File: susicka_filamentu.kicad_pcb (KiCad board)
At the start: 4 copper layers, 55 parts, among them J2 Conn_01x03, J3 Conn_01x04, J4 PJ-102AH, J5 Screw_Terminal_01x02, J6 Conn_01x04, J7 Conn_01x04, Q1 Q_NMOS_GSD, U1 RP2350A-QFN60, U2 RM2, U3 W25Q128JVS, U4 AP63203WU, Y1 Crystal_GND24

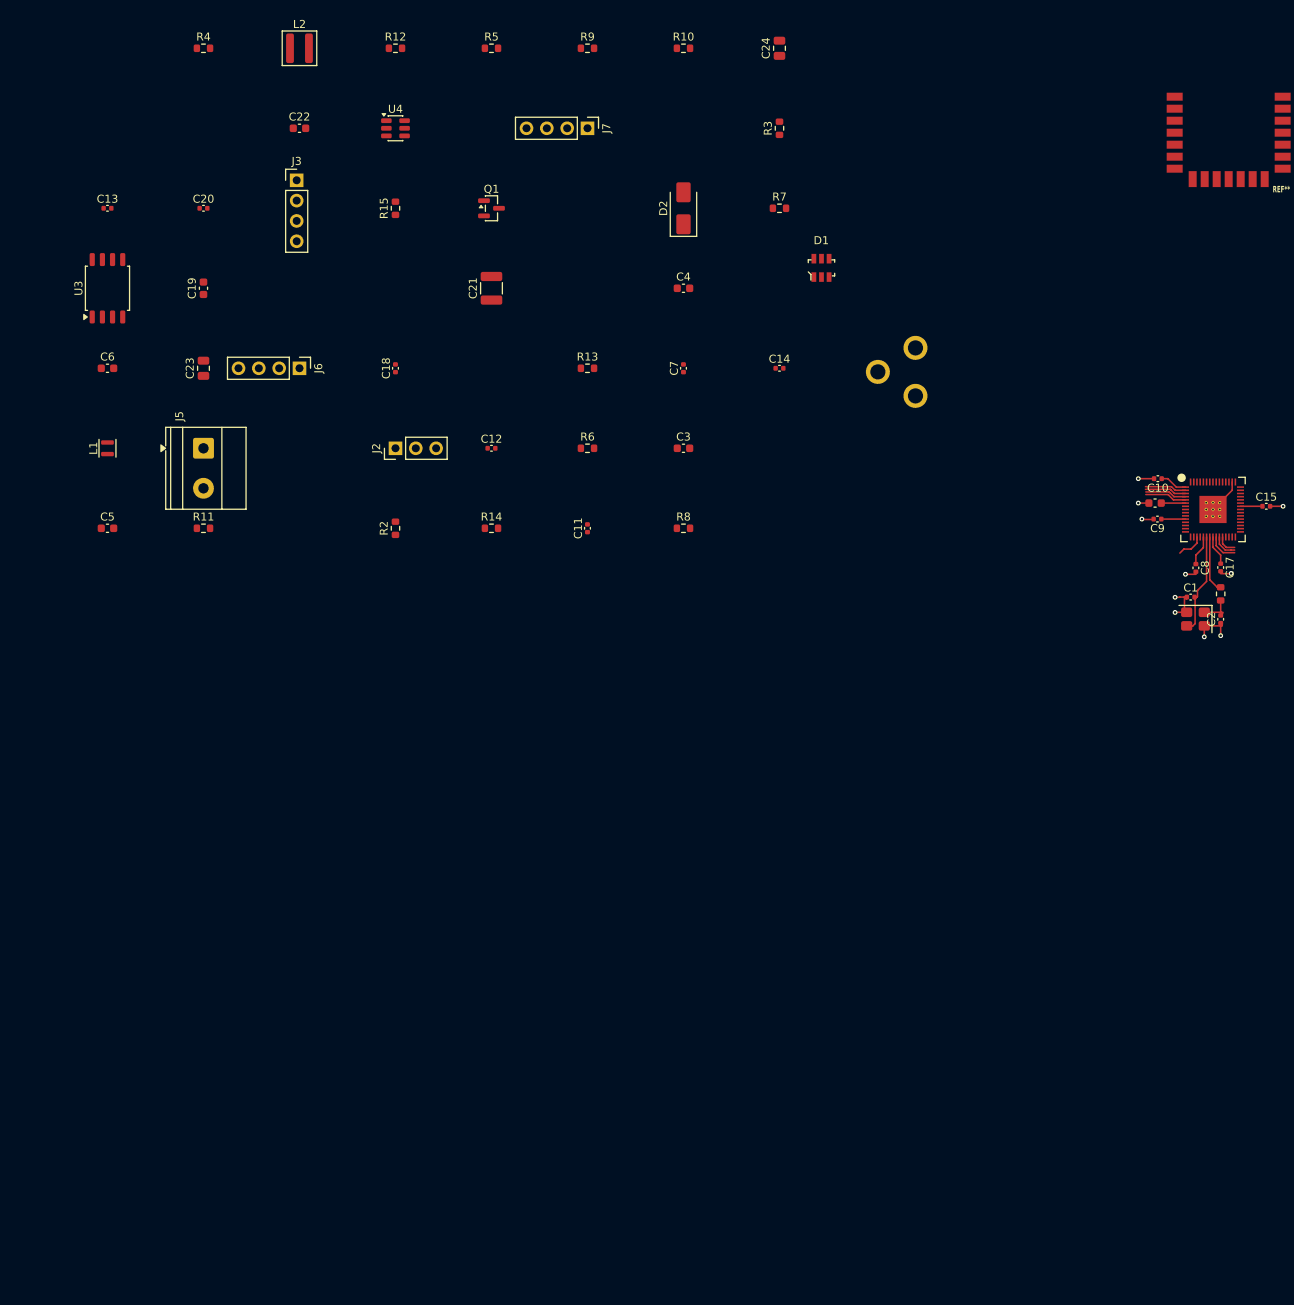
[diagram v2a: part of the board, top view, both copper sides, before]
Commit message: Add communication test points, tidy root sheet, board setup
- Test points TP6-TP19 (1 mm pads) on I2C1, I2C0, HX711, RM2 gSPI,
  heater/fan/exhaust PWM and NTC ADC, plus TP12 GND loop
- Root sheet: GPIO2-5 -> J6/J7 and GPIO24/25/29 -> RM2 now connected by
  global labels (HX711_DT/SCK, WL_DATA/CS/CLK), J6 moved
- Board updated from schematic (F8)
- Board setup: min through-hole 0.2 mm (0.25 mm vias under RP2350),
  new net class Power (1.5 mm track, 0.3 mm clearance, 0.8/0.4 via)
  for 24V_IN, 24V, fuse/heater nets

Co-Authored-By: Claude Opus 5.5 <noreply@anthropic.com>
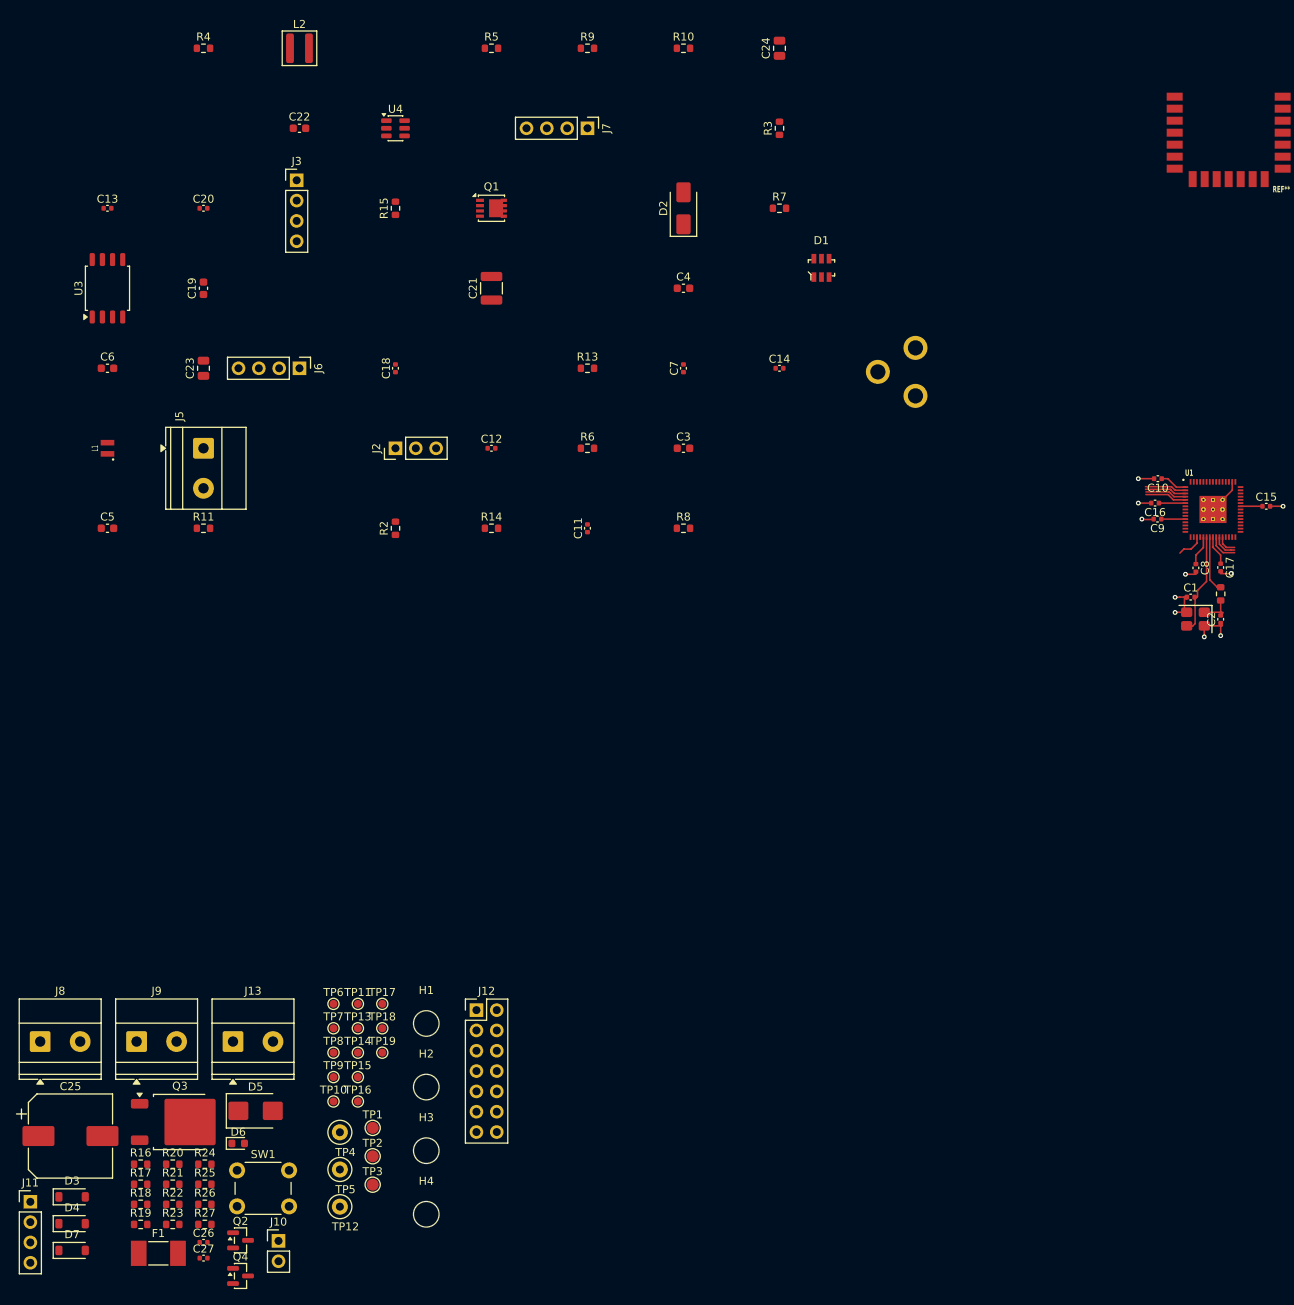
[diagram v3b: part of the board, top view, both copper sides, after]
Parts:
- removed R12: 10k, Resistor_SMD:R_0603_1608Metric
- added C25: 100uF 50V, Capacitor_SMD:CP_Elec_10x10, F.Cu at (25.0, 162.2)
- added C26: 100nF, Capacitor_SMD:C_0402_1005Metric, F.Cu at (41.7, 175.5)
- added C27: 100nF, Capacitor_SMD:C_0402_1005Metric, F.Cu at (41.7, 177.5)
- added D3: B5819W, Diode_SMD:D_SOD-123, F.Cu at (25.2, 169.8)
- added D4: BZT52C15, Diode_SMD:D_SOD-123, F.Cu at (25.2, 173.2)
- added D5: SMBJ24CA, Diode_SMD:D_SMB, F.Cu at (48.2, 159.1)
- added D6: LED zelená, LED_SMD:LED_0603_1608Metric, F.Cu at (46.0, 163.1)
- added D7: B5819W, Diode_SMD:D_SOD-123, F.Cu at (25.2, 176.5)
- added F1: 4A T, Fuse:Fuse_Littelfuse-NANO2-451_453, F.Cu at (36.0, 176.9)
- added H1: M3, MountingHole:MountingHole_3.2mm_M3, F.Cu at (69.5, 148.2)
- added H2: M3, MountingHole:MountingHole_3.2mm_M3, F.Cu at (69.5, 156.1)
- added H3: M3, MountingHole:MountingHole_3.2mm_M3, F.Cu at (69.5, 164.1)
- added H4: M3, MountingHole:MountingHole_3.2mm_M3, F.Cu at (69.5, 172.0)
- added J10: NTC 100k B3950, Connector_PinHeader_2.54mm:PinHeader_1x02_P2.54mm_Vertical, F.Cu at (51.0, 175.3)
- added J11: SHT40 #2, Connector_PinHeader_2.54mm:PinHeader_1x04_P2.54mm_Vertical, F.Cu at (20.0, 170.4)
- added J12: GPIO rezerva, Connector_PinHeader_2.54mm:PinHeader_2x07_P2.54mm_Vertical, F.Cu at (75.8, 146.5)
- added J13: Tepelna pojistka, TerminalBlock_Phoenix:TerminalBlock_Phoenix_MKDS-1,5-2_1x02_P5.00mm_Horizontal, F.Cu at (45.3, 150.4)
- added J8: Ventilator 24V, TerminalBlock_Phoenix:TerminalBlock_Phoenix_MKDS-1,5-2_1x02_P5.00mm_Horizontal, F.Cu at (21.2, 150.4)
- added J9: Odtah 24V, TerminalBlock_Phoenix:TerminalBlock_Phoenix_MKDS-1,5-2_1x02_P5.00mm_Horizontal, F.Cu at (33.3, 150.4)
- added Q2: AO3422, Package_TO_SOT_SMD:SOT-23, F.Cu at (46.3, 175.3)
- added Q3: AOD4185, Package_TO_SOT_SMD:TO-252-2, F.Cu at (38.7, 160.5)
- added Q4: AO3422, Package_TO_SOT_SMD:SOT-23, F.Cu at (46.3, 179.7)
- added R16: 100, Resistor_SMD:R_0603_1608Metric, F.Cu at (33.8, 165.7)
- added R17: 100, Resistor_SMD:R_0603_1608Metric, F.Cu at (33.8, 168.2)
- added R18: 100k, Resistor_SMD:R_0603_1608Metric, F.Cu at (33.8, 170.8)
- added R19: 10k, Resistor_SMD:R_0603_1608Metric, F.Cu at (33.8, 173.3)
- added R20: 1k, Resistor_SMD:R_0603_1608Metric, F.Cu at (37.8, 165.7)
- added R21: 4k7, Resistor_SMD:R_0603_1608Metric, F.Cu at (37.8, 168.2)
- added R22: 4k7, Resistor_SMD:R_0603_1608Metric, F.Cu at (37.8, 170.8)
- added R23: 100, Resistor_SMD:R_0603_1608Metric, F.Cu at (37.8, 173.3)
- added R24: 100k, Resistor_SMD:R_0603_1608Metric, F.Cu at (41.8, 165.7)
- added R25: 22k, Resistor_SMD:R_0603_1608Metric, F.Cu at (41.8, 168.2)
- added R26: 4k7, Resistor_SMD:R_0603_1608Metric, F.Cu at (41.8, 170.8)
- added R27: 4k7, Resistor_SMD:R_0603_1608Metric, F.Cu at (41.8, 173.3)
- added SW1: Tlacitko, Button_Switch_THT:SW_PUSH_6mm, F.Cu at (45.9, 166.5)
- added TP1: 24V, TestPoint:TestPoint_Pad_D1.5mm, F.Cu at (62.8, 161.2)
- added TP10: HX711_DT, TestPoint:TestPoint_Pad_D1.0mm, F.Cu at (57.9, 157.9)
- added TP11: HX711_SCK, TestPoint:TestPoint_Pad_D1.0mm, F.Cu at (61.0, 145.7)
- added TP12: GND, TestPoint:TestPoint_Loop_D2.50mm_Drill1.0mm, F.Cu at (58.7, 171.1)
- added TP13: WL_CLK, TestPoint:TestPoint_Pad_D1.0mm, F.Cu at (61.0, 148.8)
- added TP14: WL_CS, TestPoint:TestPoint_Pad_D1.0mm, F.Cu at (61.0, 151.8)
- added TP15: WL_DATA, TestPoint:TestPoint_Pad_D1.0mm, F.Cu at (61.0, 154.8)
- added TP16: HEAT_PWM, TestPoint:TestPoint_Pad_D1.0mm, F.Cu at (61.0, 157.9)
- added TP17: FAN_PWM, TestPoint:TestPoint_Pad_D1.0mm, F.Cu at (64.0, 145.7)
- added TP18: EXH_PWM, TestPoint:TestPoint_Pad_D1.0mm, F.Cu at (64.0, 148.8)
- added TP19: NTC_ADC, TestPoint:TestPoint_Pad_D1.0mm, F.Cu at (64.0, 151.8)
- added TP2: +3V3, TestPoint:TestPoint_Pad_D1.5mm, F.Cu at (62.8, 164.8)
- added TP3: +1V1, TestPoint:TestPoint_Pad_D1.5mm, F.Cu at (62.8, 168.3)
- added TP4: GND, TestPoint:TestPoint_Loop_D2.50mm_Drill1.0mm, F.Cu at (58.7, 161.8)
- added TP5: GND, TestPoint:TestPoint_Loop_D2.50mm_Drill1.0mm, F.Cu at (58.7, 166.4)
- added TP6: SDA, TestPoint:TestPoint_Pad_D1.0mm, F.Cu at (57.9, 145.7)
- added TP7: SCL, TestPoint:TestPoint_Pad_D1.0mm, F.Cu at (57.9, 148.8)
- added TP8: SDA0, TestPoint:TestPoint_Pad_D1.0mm, F.Cu at (57.9, 151.8)
- added TP9: SCL0, TestPoint:TestPoint_Pad_D1.0mm, F.Cu at (57.9, 154.8)
- C16: value 4,7 uF -> 100 nF; footprint Capacitor_SMD:C_0603_1608Metric -> Capacitor_SMD:C_0402_1005Metric
- J5: value Screw_Terminal_01x02 -> Topeni 24V
- J6: value Conn_01x04 -> SHT4x
- J7: value Conn_01x04 -> HX711
- L1: footprint Inductor_SMD:L_Murata_DFE201610P -> rp2350A_QFN60:L_Abracon_AOTA-B201610
- L2: value 3,9 uH -> 4,7uH
- Q1: value Q_NMOS_GSD -> SiS434DN; footprint Package_TO_SOT_SMD:SOT-23 -> susicka:Vishay_PowerPAK_1212-8_Single_GSD
- R15: value R -> 100k
- U1: footprint rp2350A_QFN60:RP2350A_QFN-60_EP_7.75x7.75_Pitch0.4mm -> rp2350A_QFN60:RP2350A_QFN-60_RPi_Minimal
- Y1: value Crystal_GND24 -> ABM8-272-T3 12MHz
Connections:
- net /RM2/RM2_CS renamed WL_CS
- net /RM2/RM2_DI renamed WL_DATA
- net /RM2/RM2_SCLK renamed WL_CLK
- net Net-(J6-Pin_3) renamed SDA
- net Net-(J6-Pin_4) renamed SCL
- net Net-(J7-Pin_3) renamed HX711_DT
- net Net-(J7-Pin_4) renamed HX711_SCK
- D2 pad 1: (no net) -> /vystupy/HEAT_V
- D2 pad 2: (no net) -> Net-(D2-A)
- J4 pad 1: 24V -> 24V_IN
- J5 pad 1: 24V -> Net-(D2-A)
- J5 pad 2: Net-(J5-Pin_2) -> /vystupy/HEAT_V
- Q1 pad 1: /GPIO14 -> Net-(Q1-G)
- Q1 pad 3: Net-(J5-Pin_2) -> Net-(D2-A)
- R15 pad 1: /GPIO14 -> Net-(Q1-G)
- U1 pad 12: unconnected-(U1-GPIO8-Pad12) -> SDA0
- U1 pad 13: unconnected-(U1-GPIO9-Pad13) -> SCL0
- U1 pad 14: unconnected-(U1-GPIO10-Pad14) -> GP10
- U1 pad 15: unconnected-(U1-GPIO11-Pad15) -> GP11
- U1 pad 16: unconnected-(U1-GPIO12-Pad16) -> EXH_PWM
- U1 pad 17: unconnected-(U1-GPIO13-Pad17) -> FAN_PWM
- U1 pad 18: /GPIO14 -> HEAT_PWM
- U1 pad 19: unconnected-(U1-GPIO15-Pad19) -> BTN
- U1 pad 27: unconnected-(U1-GPIO16-Pad27) -> GP16
- U1 pad 28: unconnected-(U1-GPIO17-Pad28) -> GP17
- U1 pad 29: unconnected-(U1-GPIO18-Pad29) -> GP18
- U1 pad 31: unconnected-(U1-GPIO19-Pad31) -> GP19
- U1 pad 32: unconnected-(U1-GPIO20-Pad32) -> GP20
- U1 pad 33: unconnected-(U1-GPIO21-Pad33) -> GP21
- U1 pad 34: unconnected-(U1-GPIO22-Pad34) -> GP22
- U1 pad 40: unconnected-(U1-GPIO26_ADC0-Pad40) -> NTC_ADC
- U1 pad 41: unconnected-(U1-GPIO27_ADC1-Pad41) -> GP27
- U1 pad 42: unconnected-(U1-GPIO28_ADC2-Pad42) -> GP28
- U2 pad 8: unconnected-(U2-GPIO0-Pad8) -> WL_GPIO0
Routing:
- net HEAT_PWM: track 0.00 -> 3.43 mm
- net /GPIO14: track 3.43 -> 0.00 mm

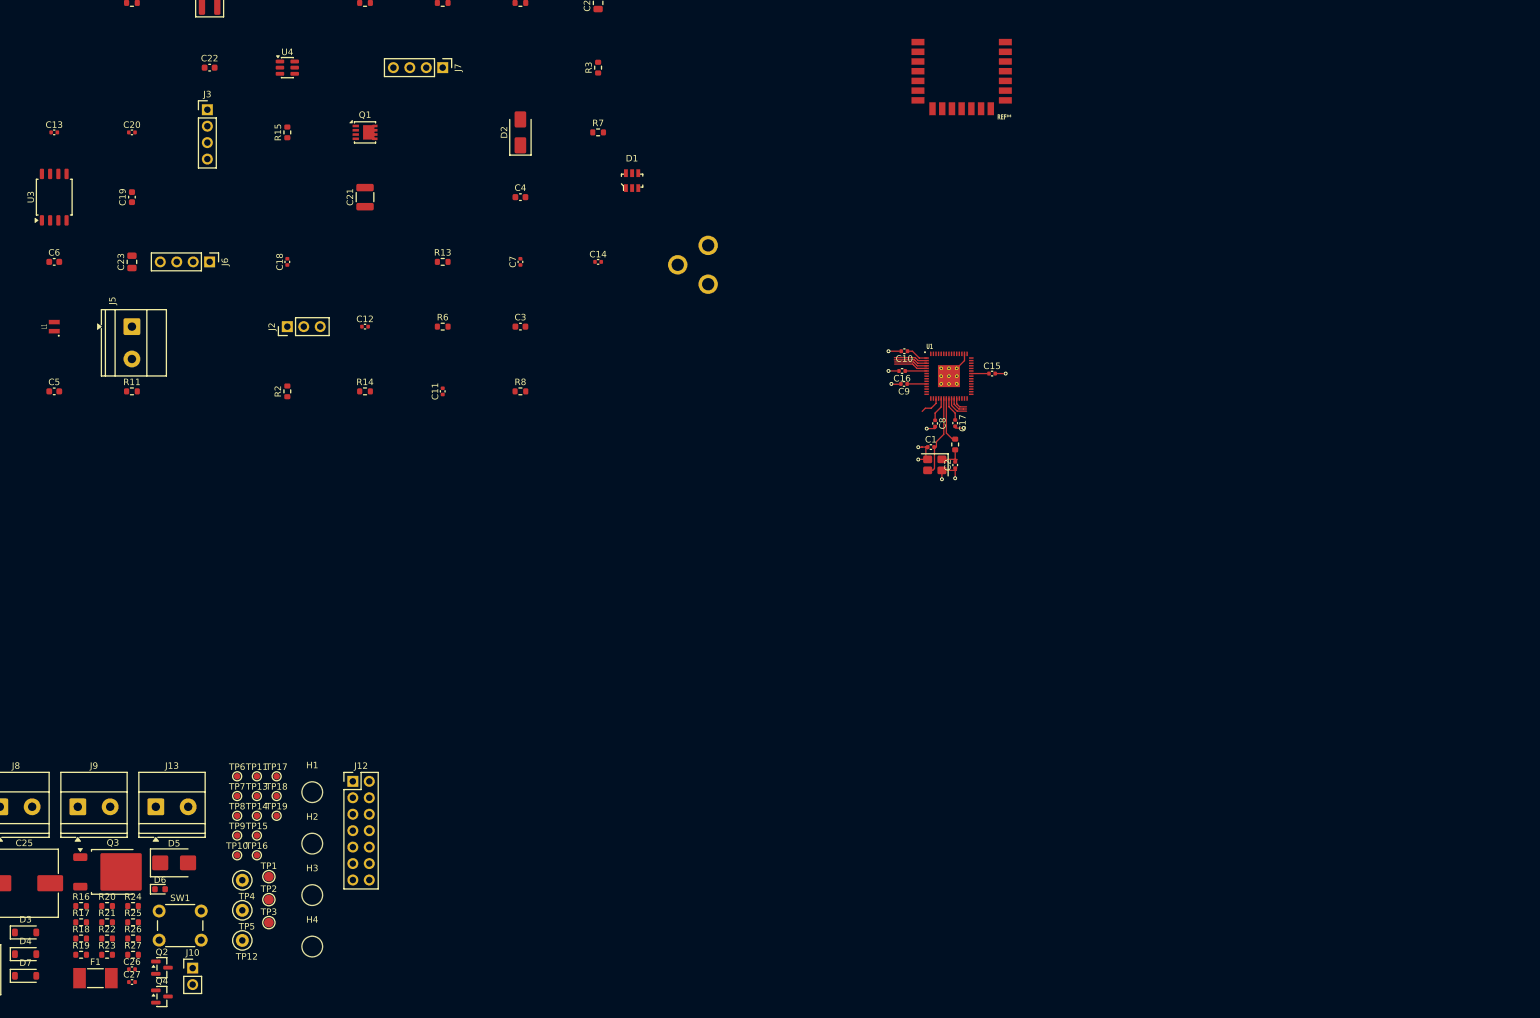
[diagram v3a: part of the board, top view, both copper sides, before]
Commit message: Layout progress, VREG per reference, SI simulation, project notes
- Board: 70x100 mm outline, mounting holes, crystal, RP2350 decoupling,
  VREG copied from RP2350A Minimal R4 (zones, priorities, PGND track),
  RM2 placement and gSPI routing (CLK 16.5 mm, DATA 14.4 mm),
  RF keep-out rule area on all copper layers, test points TP12-TP15
- C4/C5/C6/R7 in 0402; C5/C6 use susicka:C_0402_1005Metric_RPi
  (0.56 mm pad gap so VREG_LX passes under the caps)
- simulace/wl_clk: KiCad ngspice model of WL_CLK (TLINE Z0 ~94 ohm,
  td ~96 ps) for transient and AC (Bode) analysis
- CLAUDE.md and Claude subagents (.claude/agents) moved into the PCB
  branch so the project context is available on other machines
- Ignore KiCad #auto_saved_files#

Co-Authored-By: Claude Opus 5.5 <noreply@anthropic.com>
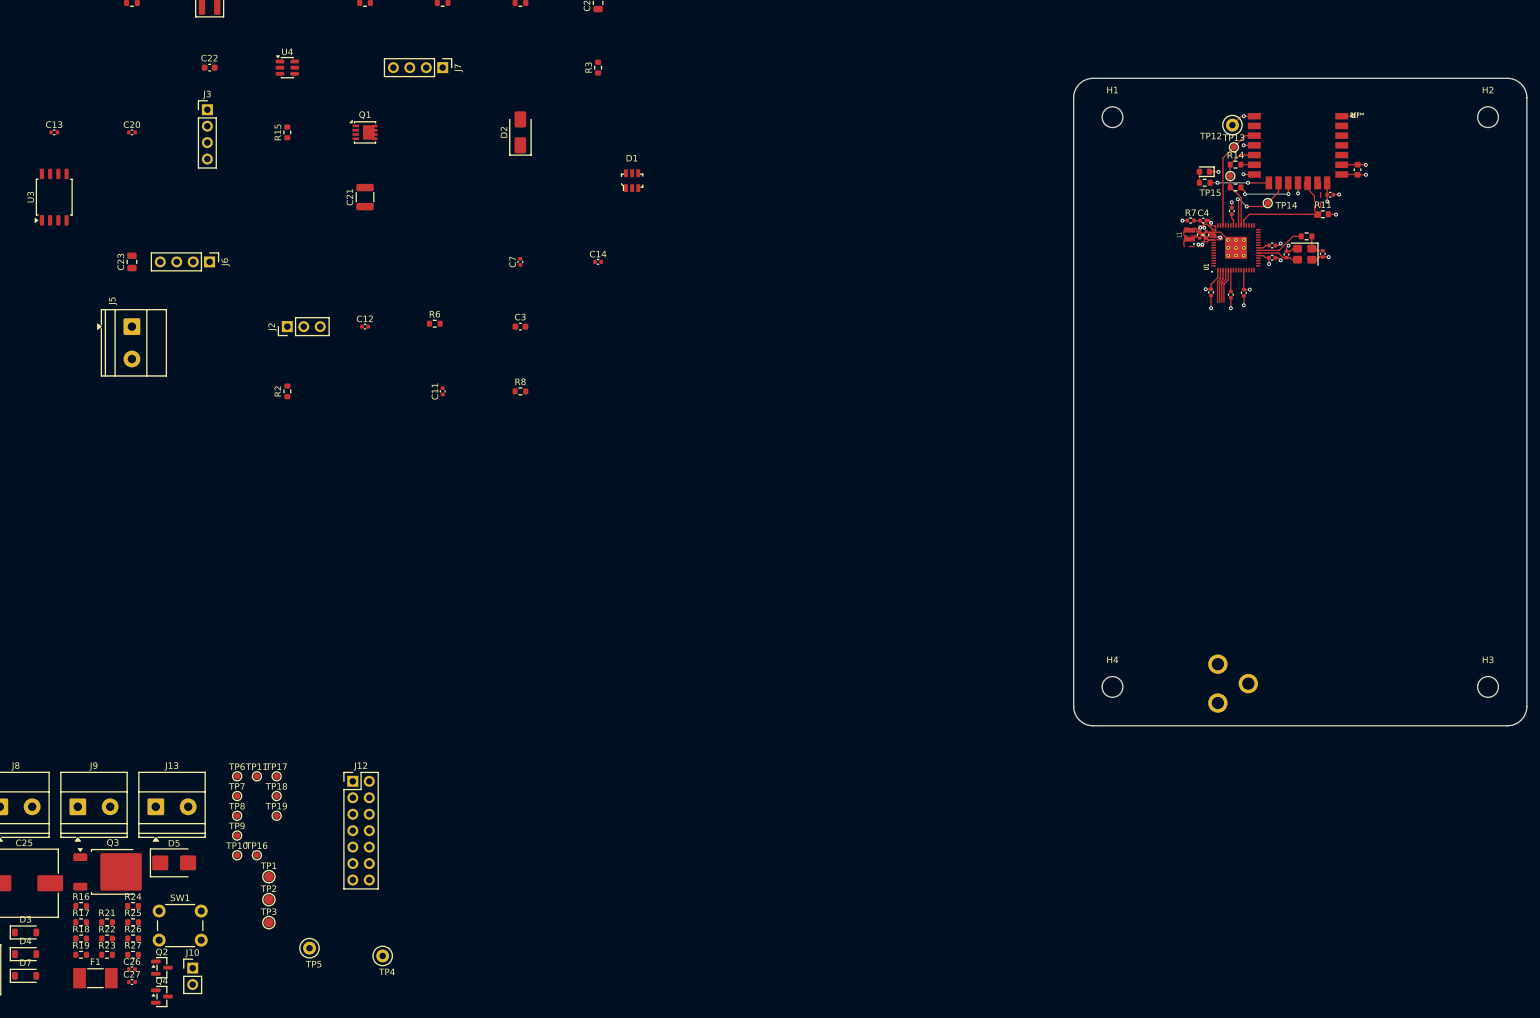
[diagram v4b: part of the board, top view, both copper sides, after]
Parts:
- C4: footprint Capacitor_SMD:C_0603_1608Metric -> Capacitor_SMD:C_0402_1005Metric
- C5, C6: footprint Capacitor_SMD:C_0603_1608Metric -> susicka:C_0402_1005Metric_RPi
- R7: footprint Resistor_SMD:R_0603_1608Metric -> Resistor_SMD:R_0402_1005Metric
- moved H2 213.5 mm to (251.1, 43.9)
- moved R20 203.0 mm to (207.3, 54.0), turned to 180 degrees
- moved TP12 198.1 mm to (211.6, 45.1)
- moved D6 195.7 mm to (207.3, 52.3), turned to 180 degrees
- moved C19 189.3 mm to (230.9, 52.0), turned to -90 degrees
- moved R11 186.0 mm to (225.6, 58.9)
- moved H3 184.4 mm to (251.1, 131.9)
- moved TP14 182.6 mm to (217.1, 57.2)
- moved TP15 181.6 mm to (211.3, 53.0)
- moved TP13 181.1 mm to (211.8, 48.5)
- moved C5 178.6 mm to (206.6, 62.1), turned to 90 degrees
- moved C6 178.0 mm to (207.6, 62.1), turned to 90 degrees
- moved L1 175.9 mm to (205.0, 62.1)
- moved H1 161.7 mm to (193.1, 43.9)
- moved C18 161.4 mm to (226.7, 55.9), turned to 0 degrees
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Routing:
- net WL_CLK: track 0.00 -> 16.7 mm
- net GND: track 22.6 -> 37.1 mm, vias 10 -> 20
- net WL_DATA: track 0.00 -> 14.5 mm
- net WL_CS: track 0.00 -> 13.2 mm, vias 0 -> 2
- net /RM2/RM2_BT_ON: track 0.00 -> 12.6 mm
- net WL_GPIO0: track 0.00 -> 10.4 mm, vias 0 -> 2
- net Net-(U2-nIRQ): track 0.00 -> 9.78 mm, vias 0 -> 2
- net +3V3: track 9.31 -> 18.1 mm, vias 0 -> 7
- net /oscillator/XIN: track 12.6 -> 6.48 mm
- net SWCLK: track 3.77 -> 0.00 mm
- net Net-(U1-VREG_AVDD): track 0.00 -> 3.64 mm
- net HEAT_PWM: track 3.43 -> 0.00 mm
- net SWDIO: track 3.12 -> 0.00 mm
- net Net-(J3-Pin_4): track 2.54 -> 0.00 mm
- net Net-(U2-DO): track 0.00 -> 2.09 mm
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- added copper zone on F.Cu, net +1V1
- added copper zone on F.Cu, net +3V3
- added copper zone on F.Cu, net /RM2/RM2_BT_ON
- added copper zone on F.Cu, net GND
- added copper zone on F.Cu, net Net-(U1-VREG_LX)
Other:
- board outline added: 70 x 100 mm
